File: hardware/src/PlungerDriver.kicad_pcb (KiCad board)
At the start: 2 copper layers, 80 x 16 mm, 30 parts, among them J1 MC 1,5/2, J2 locked, U1 16F1454, U2 TB67H450AFNG

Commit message: Refactored a bit
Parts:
- moved DS1 2.35 mm to (82.2, 17.5)
- moved R3 2.35 mm to (86.2, 17.5)
- moved R4 2.35 mm to (90.2, 17.5)
- moved R5 2.30 mm to (82.3, 28.5)
- moved R6 2.30 mm to (86.3, 28.5)
- moved R7 2.30 mm to (90.3, 28.5)
- moved C1 2.00 mm to (50.8, 21.8)
- moved C10 2.00 mm to (34.7, 23.7)
- moved C11 2.00 mm to (34.7, 26.0)
- moved C12 2.00 mm to (34.7, 28.3)
- moved C2 2.00 mm to (45.4, 21.9)
- moved C3 2.00 mm to (40.0, 22.0)
- moved C4 2.00 mm to (53.8, 16.7)
- moved C5 2.00 mm to (29.4, 19.7)
- moved C6 2.00 mm to (36.7, 19.7)
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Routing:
- net DRIVER_OUT1: track 56.2 -> 57.2 mm
- net DRIVER_RS: track 11.1 -> 12.1 mm
- net DRIVER_OUT2: track 58.2 -> 59.2 mm
- net IN_ROTARY_C: track 35.9 -> 35.3 mm
- net IN_ROTARY_A: track 40.0 -> 39.4 mm
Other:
- board size 80 x 16 mm -> 78 x 16 mm

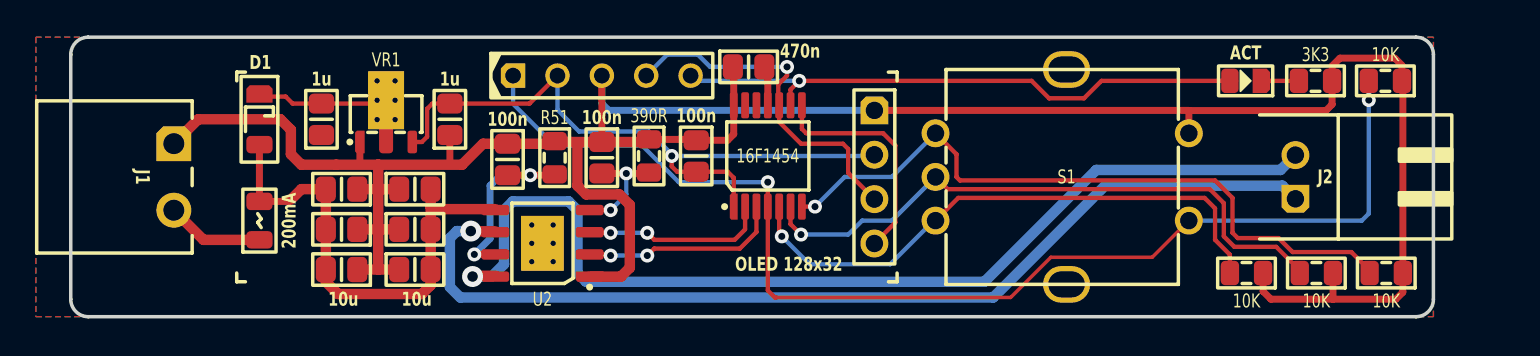
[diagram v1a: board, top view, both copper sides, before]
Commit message: Added external switch input
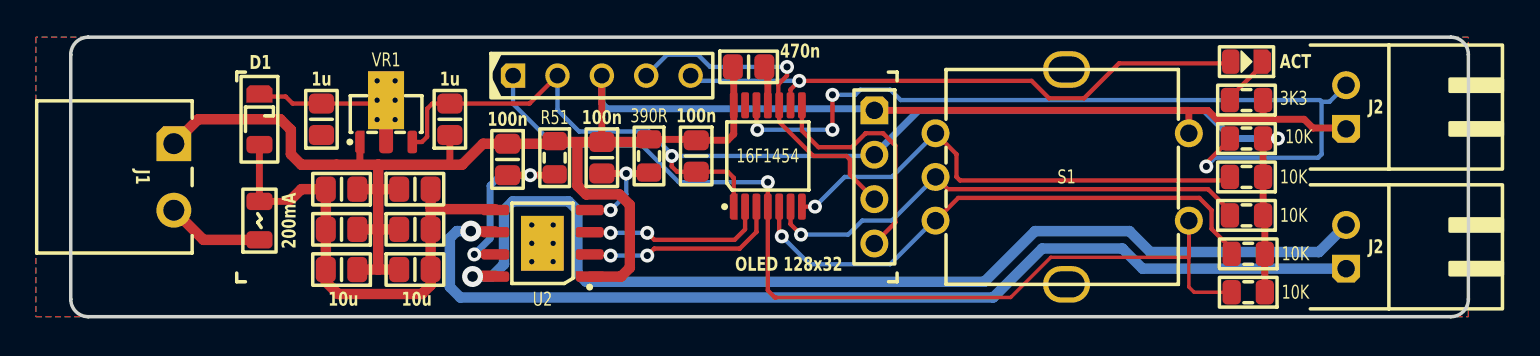
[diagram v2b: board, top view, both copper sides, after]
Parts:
- added J2: locked, Medo64:J JST XH S (2w), F.Cu at (88.0, 19.0)
- added R5: 10K, Medo64:R (0805), F.Cu at (82.4, 29.6)
- moved R7 9.71 mm to (82.3, 23.0)
- moved R4 8.61 mm to (82.3, 20.8)
- moved R6 5.19 mm to (82.3, 25.2)
- moved J2 4.94 mm to (88.0, 27.0)
- moved R3 4.10 mm to (82.3, 18.6)
- moved R5 1.10 mm to (82.4, 27.4)
- moved DS1 1.10 mm to (82.3, 16.4)
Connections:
- R4 pad 1: GND -> 3V3
- R4 pad 2: IN_ROTARY_SWITCH -> IN_EXTERNAL_SWITCH
- R5 pad 1: GND -> 3V3
- R6 pad 1: GND -> 3V3
- R7 pad 1: GND -> 3V3
- U1 pad 12: (no net) -> IN_EXTERNAL_SWITCH
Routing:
- net IN_EXTERNAL_SWITCH: track 0.00 -> 49.9 mm, vias 0 -> 4
- net 3V3: track 38.0 -> 72.3 mm, vias 1 -> 2
- net GND: track 152.6 -> 124.1 mm
- net IN_ROTARY_A: track 39.4 -> 27.9 mm
- net IN_ROTARY_SWITCH: track 68.4 -> 57.9 mm, vias 2 -> 1
- net IN_ROTARY_C: track 35.3 -> 28.8 mm
- net DRIVER_OUT2: track 59.2 -> 61.4 mm
- net DRIVER_OUT1: track 57.2 -> 58.8 mm
- net IN_ROTARY_B: track 32.9 -> 31.3 mm
- net OLED_SDO: track 13.2 -> 13.9 mm
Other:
- board size 78 x 16 mm -> 80 x 16 mm

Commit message: Changed external switch to JST PH
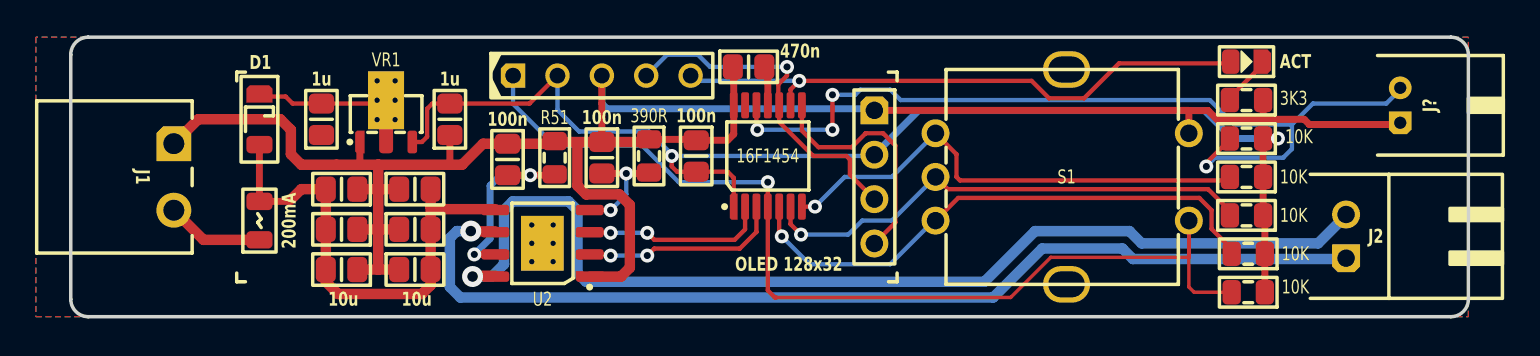
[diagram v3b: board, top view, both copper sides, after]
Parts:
- removed the J2 at (88.0, 19.0)
- added J?: S2B-PH, Medo64:J JST PH S (2w), F.Cu at (91.1, 18.9)
- moved J2 0.60 mm to (88.0, 26.4)
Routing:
- net GND: track 124.1 -> 127.2 mm
- net IN_EXTERNAL_SWITCH: track 49.9 -> 50.8 mm

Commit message: Moved connectors a bit
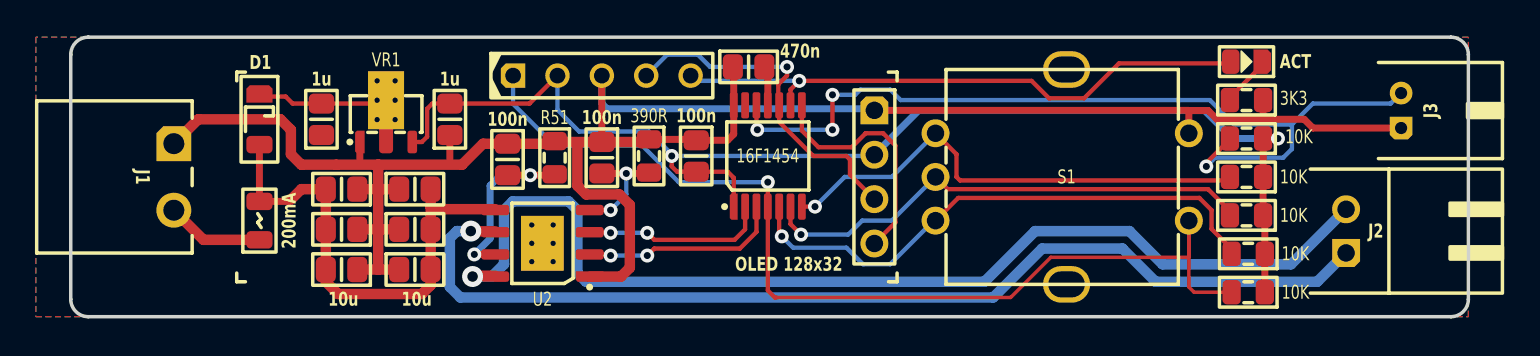
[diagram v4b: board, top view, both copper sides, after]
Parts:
- moved J3 0.30 mm to (91.2, 19.2)
- moved J2 0.30 mm to (88.0, 26.1)
- gave numbers to parts that had none: 1
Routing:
- net DRIVER_OUT1: track 58.5 -> 59.8 mm
- net DRIVER_OUT2: track 61.3 -> 62.3 mm

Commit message: Added internal switch
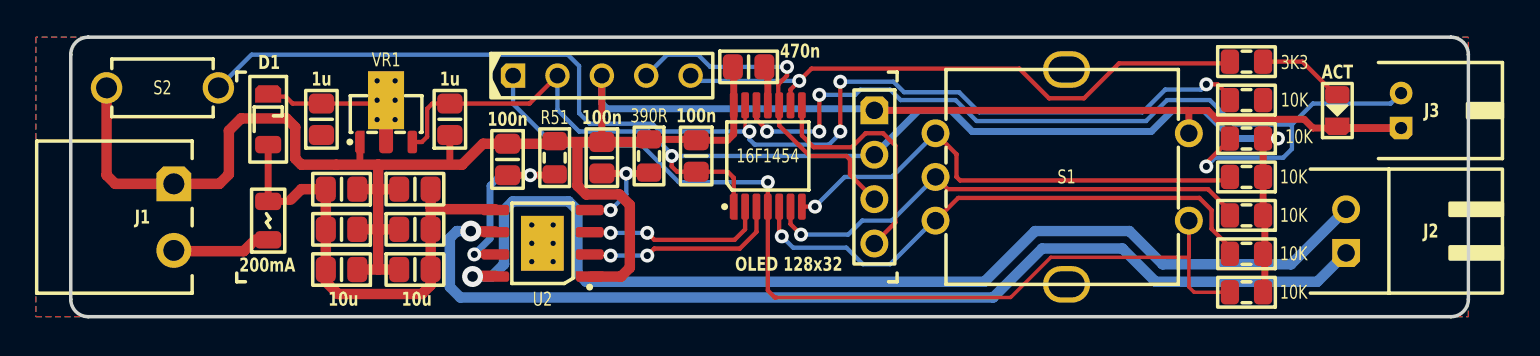
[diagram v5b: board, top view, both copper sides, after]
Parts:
- added R4: 10K, Medo64:R (0805), F.Cu at (82.3, 18.6)
- added S2: SPST, Medo64:S Tactile SPST-NO 12V 50mA 6.0x3.5x5.0mm (2w), F.Cu at (20.2, 17.9)
- moved DS1 5.91 mm to (87.5, 19.2), turned to 90 degrees
- moved J1 2.30 mm to (20.9, 25.3)
- moved R3 2.20 mm to (82.3, 16.4), turned to 0 degrees
- moved D1 0.50 mm to (26.3, 19.7)
- moved F1 0.50 mm to (26.3, 25.5)
- moved R8 0.10 mm to (82.3, 27.4)
- moved R9 0.10 mm to (82.3, 29.6)
- renumbered R4 to R5, R7 to R6, R6 to R7, R5 to R8, R5 to R9
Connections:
- DS1 pad 1: LED_ACT' -> GND
- DS1 pad 2: LED_ACT -> LED_ACT'
- R3 pad 1: GND -> LED_ACT
- U1 pad 13: (no net) -> IN_INTERNAL_SWITCH
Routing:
- net IN_INTERNAL_SWITCH: track 0.00 -> 69.0 mm, vias 0 -> 4
- net GND: track 127.3 -> 141.5 mm
- net LED_ACT': track 2.62 -> 4.94 mm
- net 3V3: track 72.3 -> 73.3 mm
- net IN_EXTERNAL_SWITCH: track 50.8 -> 51.6 mm
- net LED_ACT: track 33.4 -> 33.9 mm
- net Vfused: track 28.4 -> 27.9 mm

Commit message: Refactored to remove pulllup/input from rotary switch C line
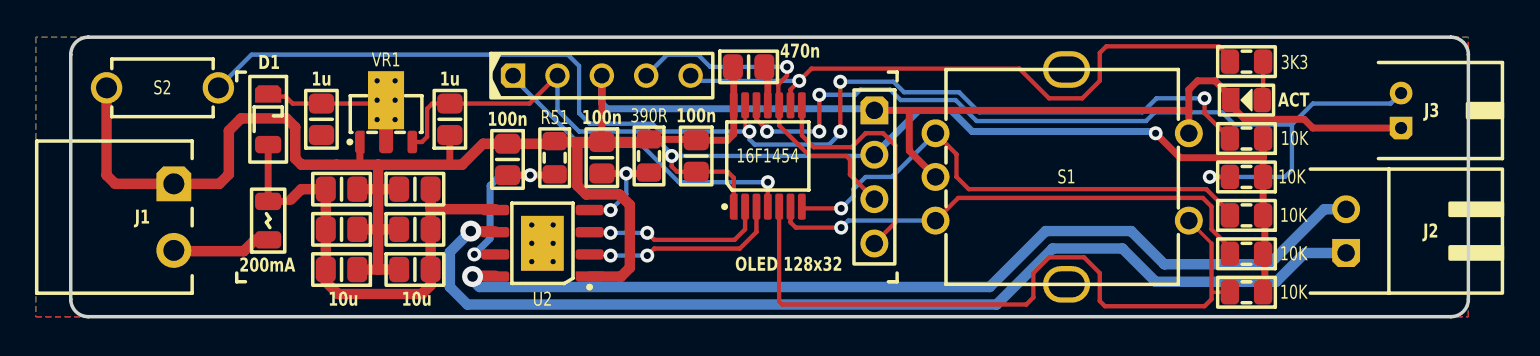
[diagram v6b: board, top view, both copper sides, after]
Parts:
- removed the R7 at (82.3, 25.2)
- moved DS1 5.23 mm to (82.3, 18.6), turned to 0 degrees
- moved R4 2.20 mm to (82.3, 20.8)
- moved R5 2.20 mm to (82.3, 23.0)
- moved R6 2.20 mm to (82.3, 25.2)
- renumbered R8 to R7, R9 to R8
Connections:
- ICSP pad 1: IN_ROTARY_SWITCH -> ICSP_VPP
- S1 pad C: IN_ROTARY_C -> GND
- U1 pad 4: IN_ROTARY_SWITCH -> ICSP_VPP
- U1 pad 5: IN_ROTARY_B -> IN_ROTARY_SWITCH
- U1 pad 6: IN_ROTARY_C -> IN_ROTARY_B
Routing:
- net IN_ROTARY_C: track 28.8 -> 0.00 mm, vias 1 -> 0
- net ICSP_VPP: track 0.00 -> 18.6 mm, vias 0 -> 1
- net IN_ROTARY_SWITCH: track 57.9 -> 43.5 mm, vias 1 -> 0
- net DRIVER_OUT2: track 62.3 -> 55.2 mm
- net LED_ACT': track 4.94 -> 2.15 mm
- net GND: track 141.5 -> 144.3 mm
- net IN_ROTARY_B: track 31.3 -> 28.8 mm
- net LED_ACT: track 33.9 -> 35.8 mm
- net IN_ROTARY_A: track 27.9 -> 29.1 mm
- net 3V3: track 73.3 -> 72.2 mm
- net IN_INTERNAL_SWITCH: track 69.0 -> 69.9 mm
- net IN_EXTERNAL_SWITCH: track 51.6 -> 50.8 mm

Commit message: Updated silkscreen
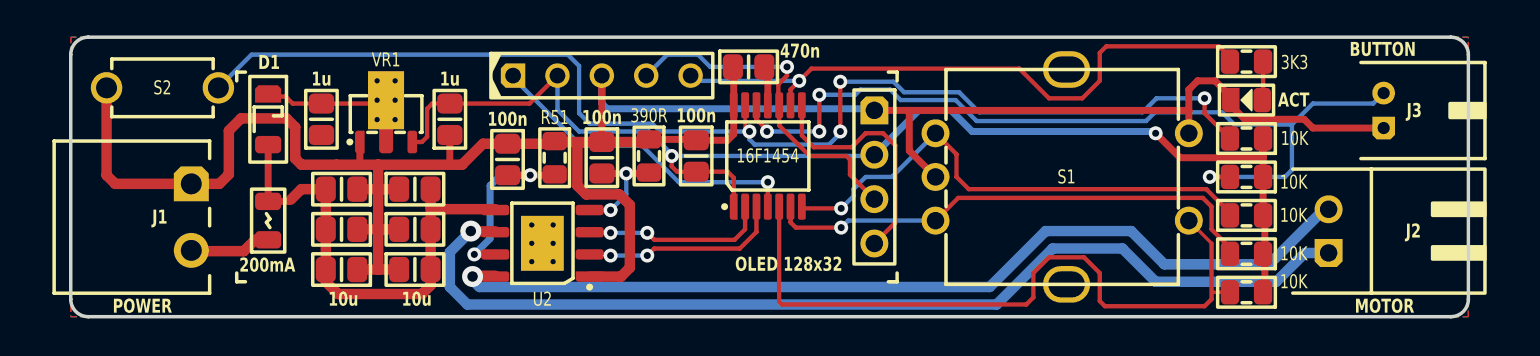
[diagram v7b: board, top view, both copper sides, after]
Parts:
- moved J1 1.00 mm to (21.9, 25.3)
- moved J2 1.00 mm to (87.0, 26.1)
- moved J3 1.00 mm to (90.2, 19.2)
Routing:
- net DRIVER_OUT2: track 55.2 -> 53.9 mm
- net IN_EXTERNAL_SWITCH: track 50.8 -> 49.8 mm
- net GND: track 144.3 -> 143.3 mm
- net Vin: track 5.12 -> 4.12 mm
- net DRIVER_OUT1: track 59.6 -> 58.6 mm
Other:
- board text added: "BUTTON"
- board text added: "MOTOR"
- board text added: "POWER"

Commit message: Added voltage divider input
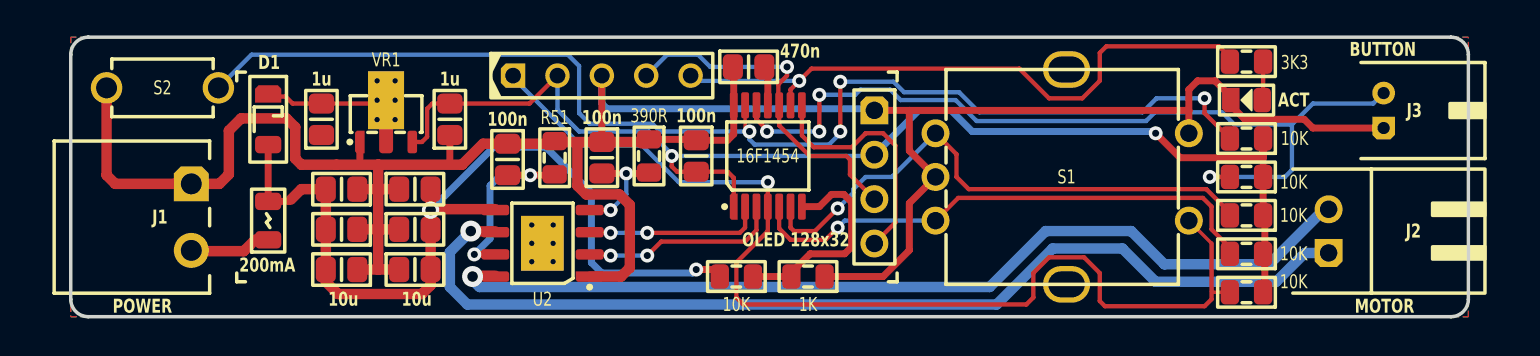
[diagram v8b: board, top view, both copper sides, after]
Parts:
- added R3: 1K, Medo64:R (0805), F.Cu at (57.2, 28.7)
- added R5: 10K, Medo64:R (0805), F.Cu at (53.1, 28.7)
- renumbered R8 to R10, R3 to R4, R4 to R6, R5 to R7, R6 to R8, R7 to R9
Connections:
- ICSP pad 1: ICSP_VPP -> IN_ROTARY_SWITCH
- U1 pad 4: ICSP_VPP -> IN_ROTARY_SWITCH
- U1 pad 5: IN_ROTARY_SWITCH -> IN_ROTARY_B
- U1 pad 6: IN_ROTARY_B -> IN_ROTARY_A
- U1 pad 7: IN_ROTARY_A -> IN_ADC_INPUT_VOLTAGE
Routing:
- net Vfused: track 27.9 -> 51.3 mm, vias 0 -> 2
- net IN_ROTARY_SWITCH: track 43.5 -> 65.0 mm, vias 0 -> 1
- net ICSP_VPP: track 18.5 -> 0.00 mm, vias 1 -> 0
- net IN_ADC_INPUT_VOLTAGE: track 0.00 -> 12.1 mm
- net GND: track 143.3 -> 153.6 mm
- net IN_ROTARY_A: track 29.1 -> 31.7 mm
- net IN_ROTARY_B: track 28.7 -> 30.3 mm
